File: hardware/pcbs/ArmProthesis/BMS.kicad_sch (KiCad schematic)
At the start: 52 parts, among them J1 XT60-M, J2 XT60-F, J3 4-1971800-1, Q1 BSC014N04LSIATMA1, Q2 BSC014N04LSIATMA1, Q3 BSS84, SW1 CK_KMS2xxG, SW2 CK_KMS2xxG, SW4 CK_KMS2xxG, U1 BQ76920PW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

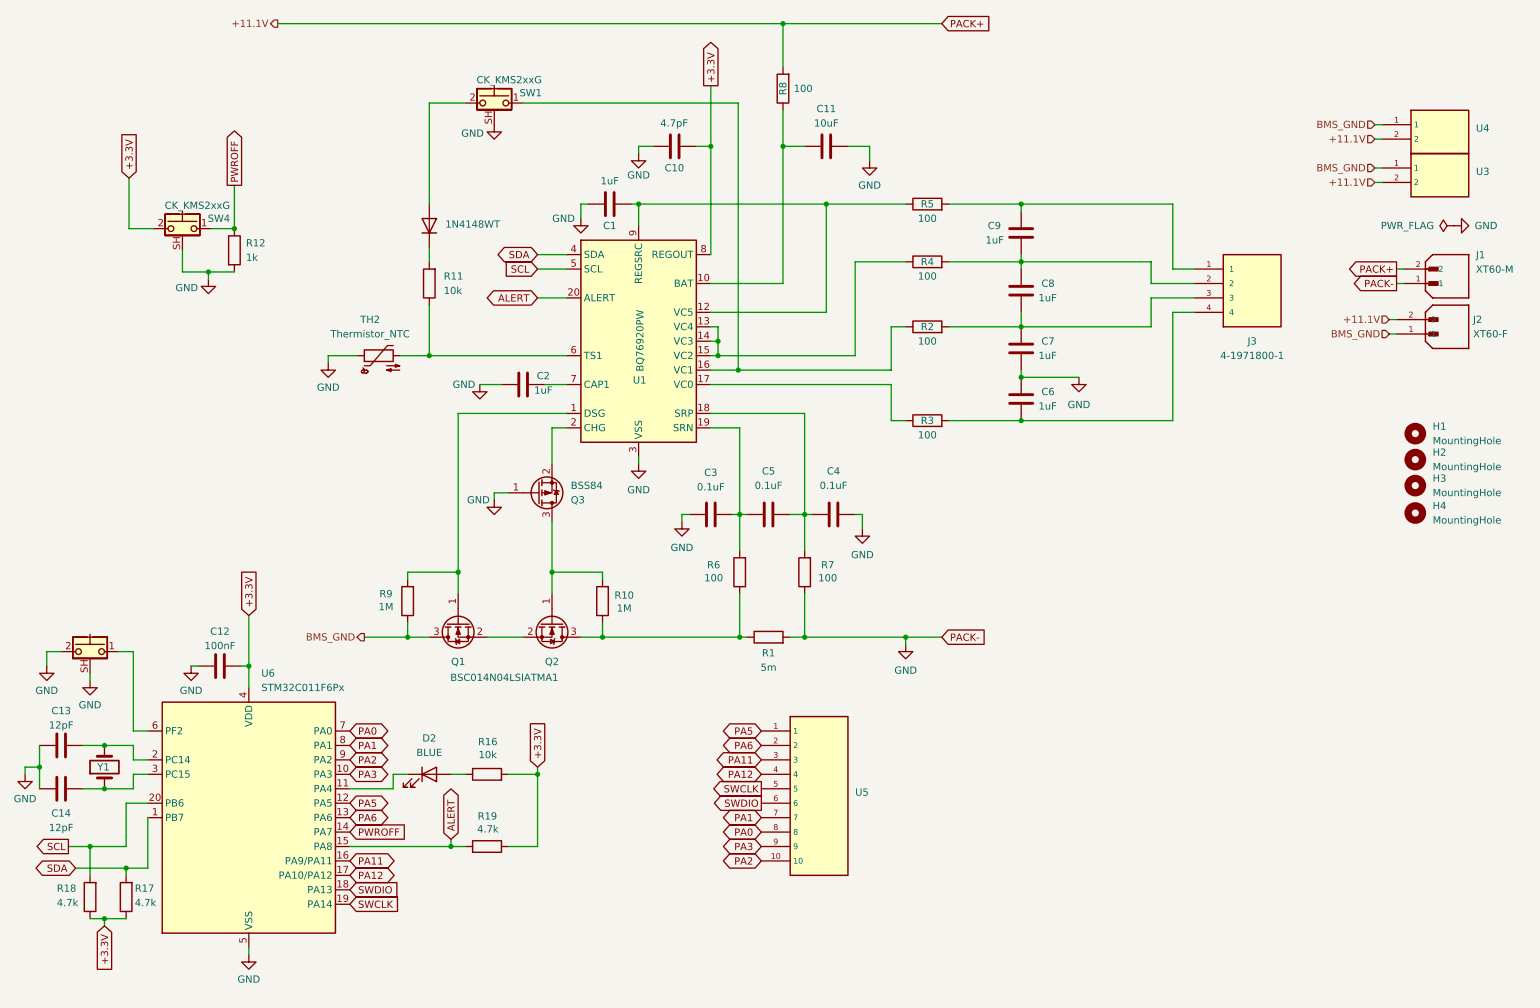
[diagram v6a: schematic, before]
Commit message: Fixed compatibility of connectors  + new BMS chip
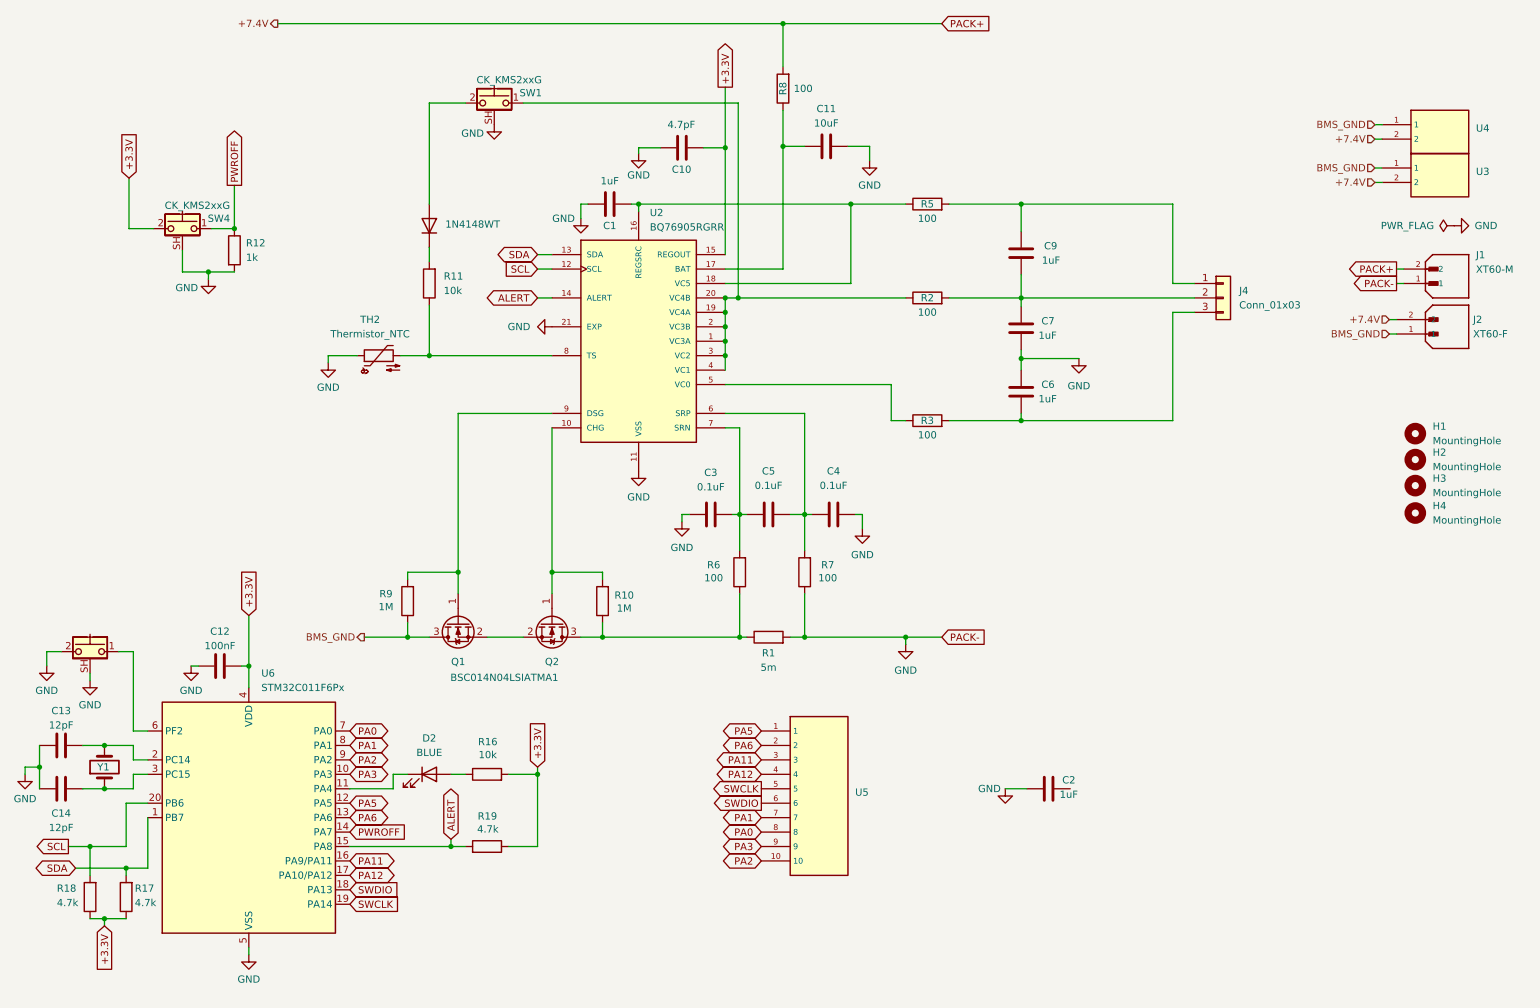
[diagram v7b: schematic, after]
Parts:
- removed C8: 1uF, Capacitor_SMD:C_0603_1608Metric, symbol Device:C
- removed J3: 4-1971800-1, Connector_JST:JST_XH_S4B-XH-A_1x04_P2.50mm_Horizontal, symbol headers:4-1971800-1
- removed Q3: BSS84, Package_TO_SOT_SMD:SOT-23, symbol Transistor_FET:BSS84
- removed R4: 100, Resistor_SMD:R_0402_1005Metric, symbol Device:R
- removed U1: BQ76920PW, Package_SO:TSSOP-20_4.4x6.5mm_P0.65mm, symbol Battery_Management:BQ76920PW
- added J4: Conn_01x03, Connector_JST:JST_GH_BM03B-GHS-TBT_1x03-1MP_P1.25mm_Vertical, symbol Connector_Generic:Conn_01x03
- added U2: BQ76905RGRR, BQ76905RGRR:IC_BQ76905RGRR, symbol OP AMPS:BQ76905RGRR
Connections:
- net +3.3V: now also U2.15 (REGOUT)
- net ALERT: now also U2.14 (ALERT)
- net GND: now also U2.11 (VSS), U2.21 (EXP)
- net SCL: now also U2.12 (SCL)
- net SDA: now also U2.13 (SDA)
- net at C11.2, R8.1: now also U2.17 (BAT)
- net at C1.2, R5.1: now also U2.16 (REGSRC), U2.18 (VC5)
- net at C9.1, R5.2: now also J4.1 (Pin_1)
- net at C9.2: now also C7.1, R2.2, J4.2 (Pin_2)
- net at C6.2, R3.2: now also J4.3 (Pin_3)
- net at Q2.1 (G), R10.2: now also U2.10 (CHG)
- net at C4.2, C5.2, R7.2: now also U2.6 (SRP)
- net at Q1.1 (G), R9.2: now also U2.9 (DSG)
- net at R2.1, SW1.1: now also U2.1 (VC3A), U2.19 (VC4A), U2.2 (VC3B), U2.20 (VC4B), U2.3 (VC2), U2.4 (VC1)
- net at R3.1: now also U2.5 (VC0)
- net at C3.2, C5.1, R6.2: now also U2.7 (SRN)
- net at R11.1, TH2.2: now also U2.8 (TS)
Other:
- moved on the sheet: C10, C2, C6, C7, C9, R2

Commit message: bms V0.7 with BQ76905
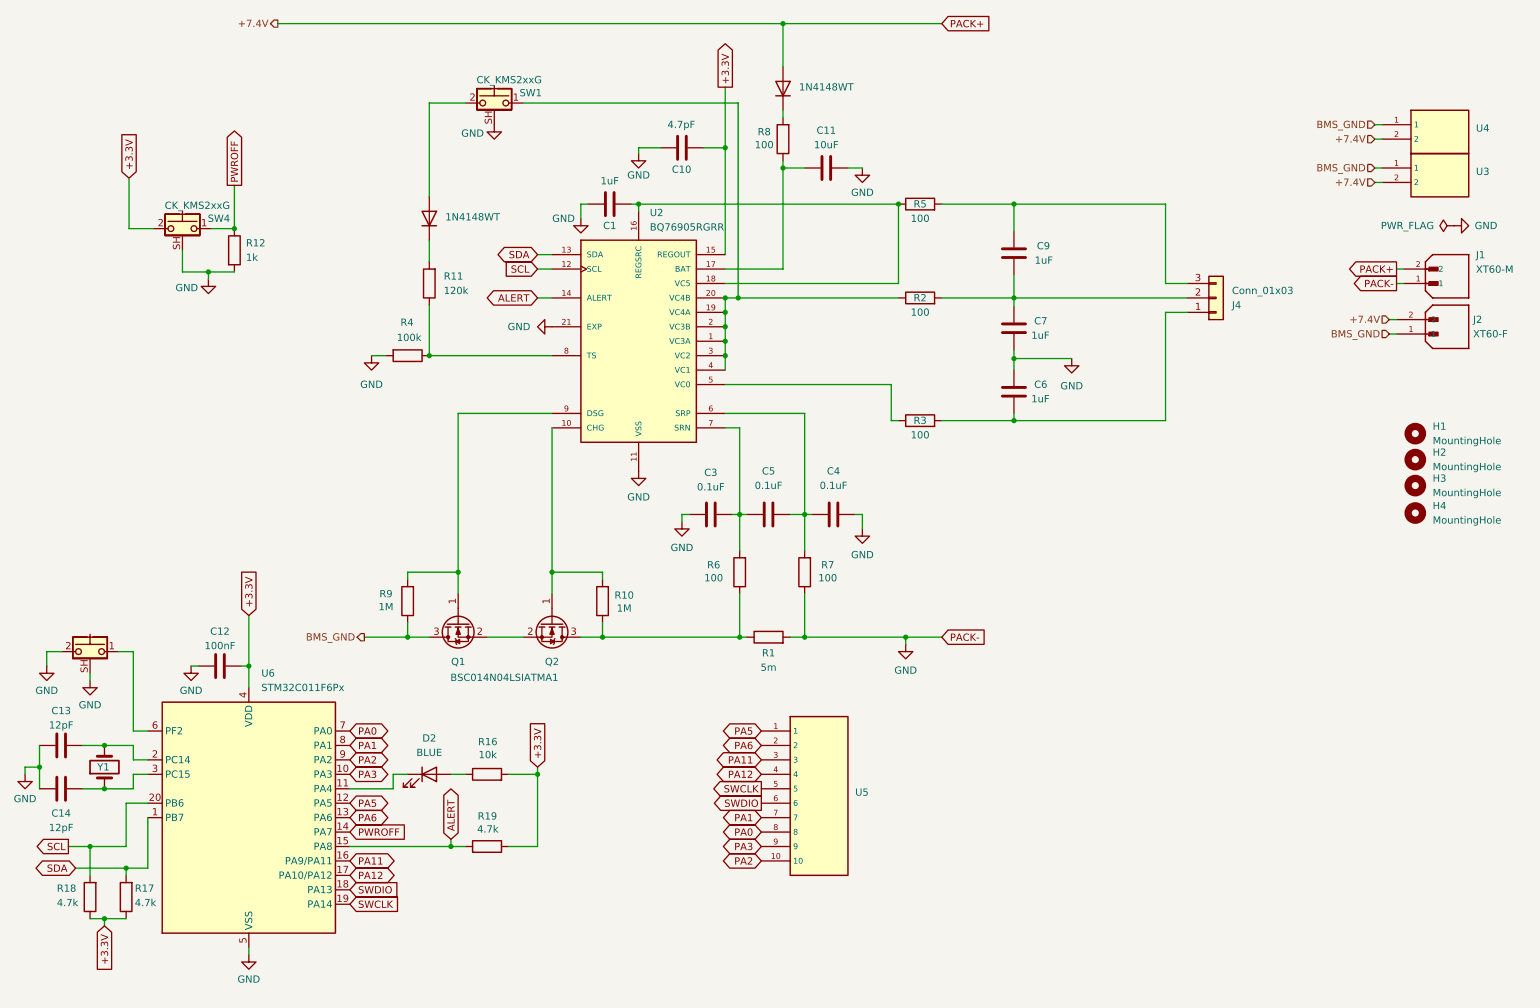
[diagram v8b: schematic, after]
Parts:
- removed C2: 1uF, Capacitor_SMD:C_0603_1608Metric, symbol Device:C
- removed TH2: Thermistor_NTC, Resistor_SMD:R_0603_1608Metric_Pad0.98x0.95mm_HandSolder, symbol Device:Thermistor_NTC
- added D3: 1N4148WT, Diode_SMD:D_SOD-523, symbol Diode:1N4148WT
- added R4: 100k, Resistor_SMD:R_0402_1005Metric, symbol Device:R
- C11: footprint Capacitor_SMD:C_1210_3225Metric -> Capacitor_SMD:C_1206_3216Metric
- R11: value 10k -> 120k
- U2: footprint BQ76905RGRR:IC_BQ76905RGRR -> BMS:BQ76905RGRR
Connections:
- net GND: now also R4.2
- net PACK+: now also D3.2 (A); no longer R8.2
- net at R11.1, U2.8 (TS): now also R4.1
- net at C9.1, R5.2: now also J4.3 (Pin_3); no longer J4.1 (Pin_1)
- net at C6.2, R3.2: now also J4.1 (Pin_1); no longer J4.3 (Pin_3)
- new net: D3.1 (K), R8.2
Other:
- moved on the sheet: C11, C6, C7, C9, J4, R2, R3, R5, R8
